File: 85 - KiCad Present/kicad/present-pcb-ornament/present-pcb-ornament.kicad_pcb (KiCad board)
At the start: 2 copper layers, 91.4 x 96.4 mm, 2 parts

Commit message: post stream
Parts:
- removed G*** (x2): LOGO, vector-files:inside zones
- added Ref**: Val**, svg2shen export:inky escaped, F.Cu at (157.7, 100.6)
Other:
- board size 91.4 x 96.4 mm -> 62.8 x 74.6 mm

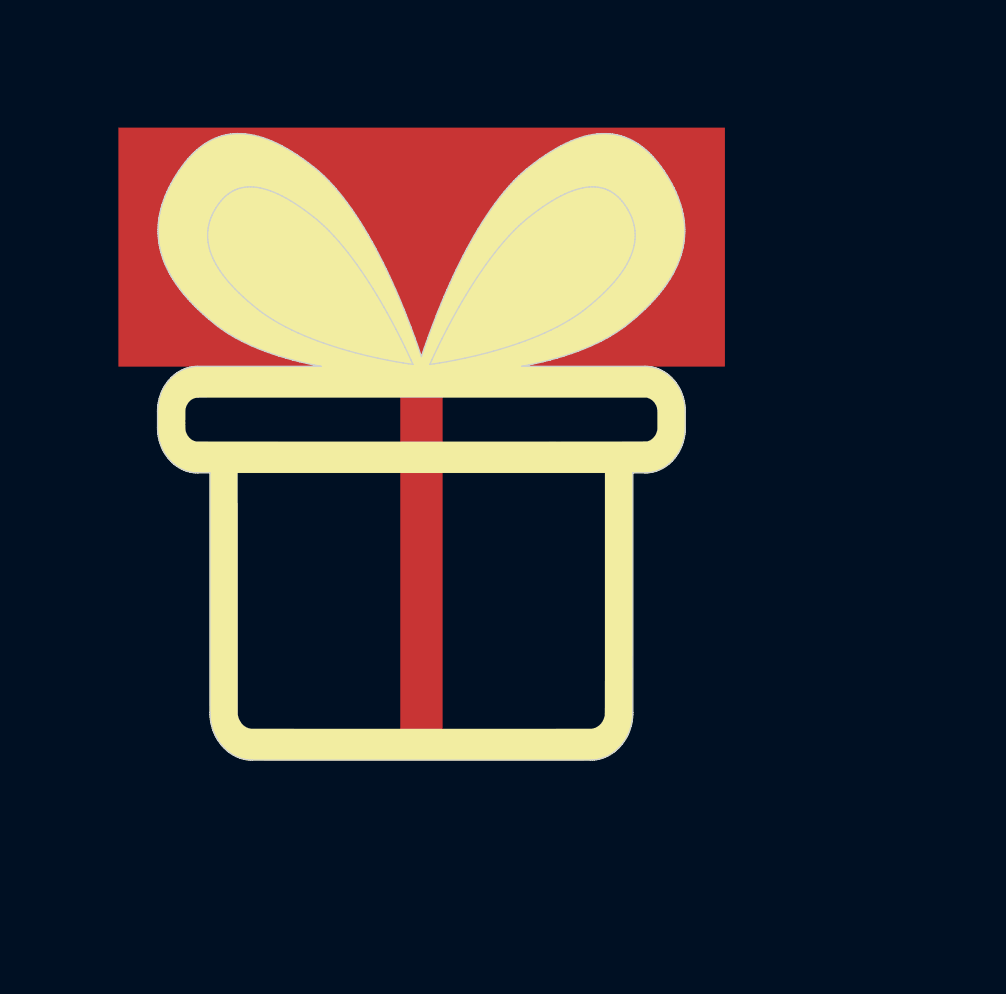
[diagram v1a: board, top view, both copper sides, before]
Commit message: new approach: atmega8 design
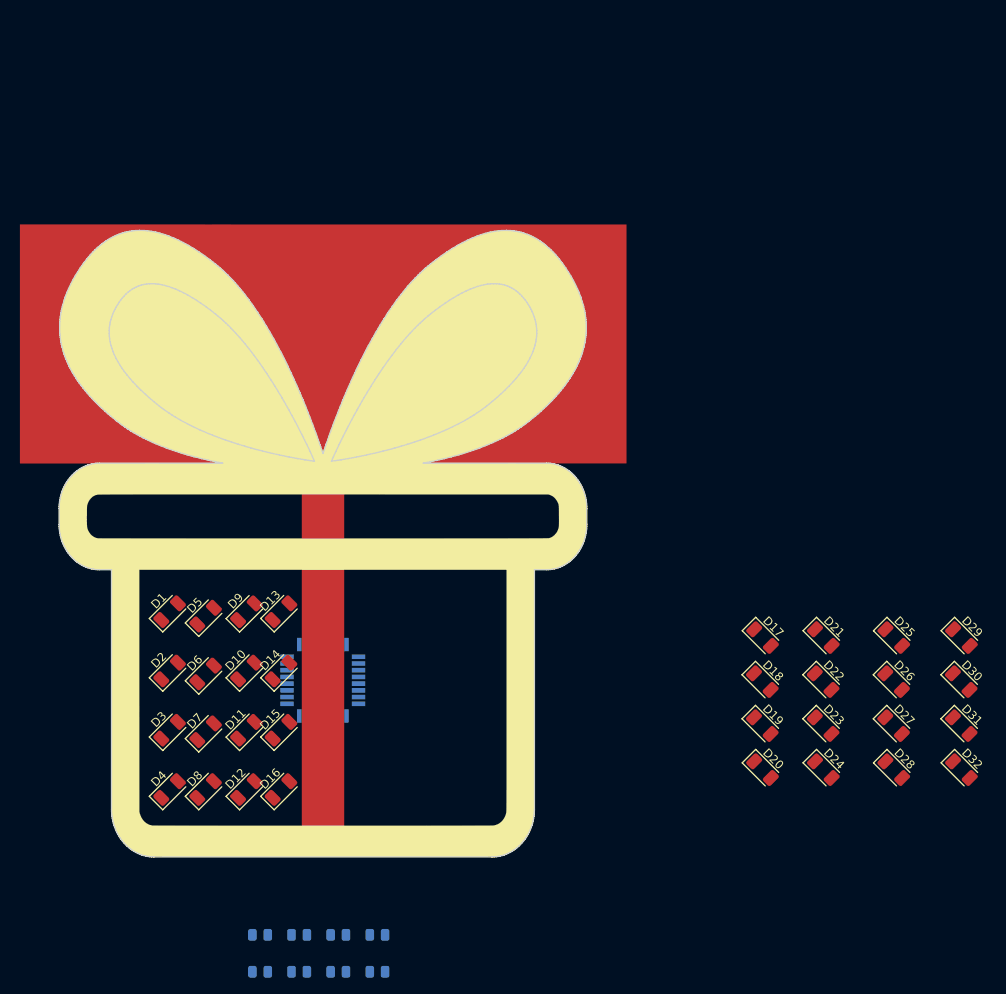
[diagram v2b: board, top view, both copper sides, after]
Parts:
- removed Ref**: Val**, svg2shen export:inky escaped
- added D1: GRN, LED_SMD:LED_1206_3216Metric, F.Cu at (129.1, 122.6)
- added D10: GRN, LED_SMD:LED_1206_3216Metric, F.Cu at (138.3, 129.7)
- added D11: GRN, LED_SMD:LED_1206_3216Metric, F.Cu at (138.3, 136.7)
- added D12: GRN, LED_SMD:LED_1206_3216Metric, F.Cu at (138.3, 143.8)
- added D13: GRN, LED_SMD:LED_1206_3216Metric, F.Cu at (142.4, 122.6)
- added D14: GRN, LED_SMD:LED_1206_3216Metric, F.Cu at (142.4, 129.7)
- added D15: GRN, LED_SMD:LED_1206_3216Metric, F.Cu at (142.4, 136.7)
- added D16: GRN, LED_SMD:LED_1206_3216Metric, F.Cu at (142.4, 143.8)
- added D17: GRN, LED_SMD:LED_1206_3216Metric, F.Cu at (199.7, 125.7)
- added D18: GRN, LED_SMD:LED_1206_3216Metric, F.Cu at (199.7, 130.9)
- added D19: GRN, LED_SMD:LED_1206_3216Metric, F.Cu at (199.7, 136.2)
- added D2: GRN, LED_SMD:LED_1206_3216Metric, F.Cu at (129.1, 129.7)
- added D20: GRN, LED_SMD:LED_1206_3216Metric, F.Cu at (199.7, 141.4)
- added D21: GRN, LED_SMD:LED_1206_3216Metric, F.Cu at (206.9, 125.7)
- added D22: GRN, LED_SMD:LED_1206_3216Metric, F.Cu at (206.9, 130.9)
- added D23: GRN, LED_SMD:LED_1206_3216Metric, F.Cu at (206.9, 136.2)
- added D24: GRN, LED_SMD:LED_1206_3216Metric, F.Cu at (206.9, 141.4)
- added D25: GRN, LED_SMD:LED_1206_3216Metric, F.Cu at (215.3, 125.7)
- added D26: GRN, LED_SMD:LED_1206_3216Metric, F.Cu at (215.3, 130.9)
- added D27: GRN, LED_SMD:LED_1206_3216Metric, F.Cu at (215.3, 136.2)
- added D28: GRN, LED_SMD:LED_1206_3216Metric, F.Cu at (215.3, 141.4)
- added D29: GRN, LED_SMD:LED_1206_3216Metric, F.Cu at (223.4, 125.7)
- added D3: GRN, LED_SMD:LED_1206_3216Metric, F.Cu at (129.1, 136.7)
- added D30: GRN, LED_SMD:LED_1206_3216Metric, F.Cu at (223.4, 130.9)
- added D31: GRN, LED_SMD:LED_1206_3216Metric, F.Cu at (223.4, 136.2)
- added D32: GRN, LED_SMD:LED_1206_3216Metric, F.Cu at (223.4, 141.4)
- added D4: GRN, LED_SMD:LED_1206_3216Metric, F.Cu at (129.1, 143.8)
- added D5: GRN, LED_SMD:LED_1206_3216Metric, F.Cu at (133.4, 123.1)
- added D6: GRN, LED_SMD:LED_1206_3216Metric, F.Cu at (133.4, 130.0)
- added D7: GRN, LED_SMD:LED_1206_3216Metric, F.Cu at (133.4, 136.9)
- added D8: GRN, LED_SMD:LED_1206_3216Metric, F.Cu at (133.4, 143.8)
- added D9: GRN, LED_SMD:LED_1206_3216Metric, F.Cu at (138.3, 122.6)
- added H1: PCB, svg2shen export:inky escaped, F.Cu at (146.0, 112.1)
- added R1: R_0805, Resistor_SMD:R_0805_2012Metric, B.Cu at (153.9, 161.1)
- added R2: R_0805, Resistor_SMD:R_0805_2012Metric, B.Cu at (149.2, 161.1)
- added R3: R_0805, Resistor_SMD:R_0805_2012Metric, B.Cu at (144.6, 161.1)
- added R4: R_0805, Resistor_SMD:R_0805_2012Metric, B.Cu at (139.9, 161.1)
- added R5: R_0805, Resistor_SMD:R_0805_2012Metric, B.Cu at (153.9, 165.5)
- added R6: R_0805, Resistor_SMD:R_0805_2012Metric, B.Cu at (149.2, 165.5)
- added R7: R_0805, Resistor_SMD:R_0805_2012Metric, B.Cu at (144.6, 165.5)
- added R8: R_0805, Resistor_SMD:R_0805_2012Metric, B.Cu at (139.9, 165.5)
- added U1: ATmega8A-AU, Package_QFP:TQFP-32_7x7mm_P0.8mm, B.Cu at (147.4, 130.8)
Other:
- outline, holes or cut-outs redrawn

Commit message: Stupid GND is Stupid
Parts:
- added C1: 10u, Capacitor_SMD:C_0805_2012Metric, B.Cu at (145.8, 126.0)
- added C2: 10u, Capacitor_SMD:C_0805_2012Metric, B.Cu at (138.0, 108.1)
- added D33: Batt, My Libraries:LED_1206_3216Metric-NoSilk, B.Cu at (139.4, 126.2)
- added D34: RED, My Libraries:LED_1206_3216Metric-NoSilk, F.Cu at (122.9, 111.3)
- added D35: RED, My Libraries:LED_1206_3216Metric-NoSilk, F.Cu at (129.1, 111.3)
- added D36: RED, My Libraries:LED_1206_3216Metric-NoSilk, F.Cu at (135.3, 111.3)
- added D37: RED, My Libraries:LED_1206_3216Metric-NoSilk, F.Cu at (141.5, 111.3)
- added D38: RED, My Libraries:LED_1206_3216Metric-NoSilk, F.Cu at (153.2, 111.3)
- added D39: RED, My Libraries:LED_1206_3216Metric-NoSilk, F.Cu at (159.3, 111.3)
- added D40: RED, My Libraries:LED_1206_3216Metric-NoSilk, F.Cu at (165.5, 111.3)
- added D41: RED, My Libraries:LED_1206_3216Metric-NoSilk, F.Cu at (171.7, 111.3)
- added J1: Batt, Connector_JST:JST_PH_S2B-PH-SM4-TB_1x02-1MP_P2.00mm_Horizontal, B.Cu at (146.2, 109.5)
- added J2: ISP, My Libraries:PinHeader_1x06_P2.54mm_SMD_Field, B.Cu at (124.5, 132.6)
- added R10: 0, Resistor_SMD:R_1206_3216Metric, B.Cu at (131.1, 116.3)
- added R11: 0, Resistor_SMD:R_1206_3216Metric, B.Cu at (135.8, 116.2)
- added R12: 0, Resistor_SMD:R_1206_3216Metric, B.Cu at (128.4, 116.2)
- added R13: 0, Resistor_SMD:R_1206_3216Metric, B.Cu at (173.6, 113.0)
- added R14: 0, Resistor_SMD:R_1206_3216Metric, B.Cu at (129.0, 107.2)
- added R15: 0, Resistor_SMD:R_1206_3216Metric, B.Cu at (118.5, 126.6)
- added R16: 0, Resistor_SMD:R_0805_2012Metric, B.Cu at (141.4, 128.7)
- added R17: 0, Resistor_SMD:R_0805_2012Metric, B.Cu at (148.7, 129.3)
- added R18: 0, Resistor_SMD:R_0805_2012Metric, B.Cu at (148.7, 135.8)
- added R19: 0, Resistor_SMD:R_1206_3216Metric, B.Cu at (140.2, 108.1)
- added R9: 1K, Resistor_SMD:R_0805_2012Metric, B.Cu at (135.0, 126.4)
- added SW1: PWR, My Libraries:SW_SPDT_PCM12-no-mounts, B.Cu at (156.7, 107.2)
- added SW2: RESET, My Libraries:SW_Push_CK_PTS525_SM15, B.Cu at (120.8, 111.1)
- D1: value GRN -> RED; footprint LED_SMD:LED_1206_3216Metric -> My Libraries:LED_1206_3216Metric-NoSilk
- D10, D11, D12, D13, D14, D15, D16, D17, D18, D19, D2, D20, D21, D22, D23, D24, D25, D26, D27, D28, D29, D3, D30, D31, D32, D4, D5, D6, D7, D8, D9: footprint LED_SMD:LED_1206_3216Metric -> My Libraries:LED_1206_3216Metric-NoSilk
- moved D29 57.4 mm to (166.0, 122.6)
- moved D32 57.4 mm to (166.0, 143.8)
- moved D30 57.4 mm to (166.0, 129.7)
- moved D31 57.3 mm to (166.0, 136.8)
- moved R8 54.6 mm to (166.1, 117.6)
- moved D25 53.8 mm to (161.6, 122.6)
- moved D28 53.8 mm to (161.6, 143.8)
- moved D26 53.7 mm to (161.6, 129.7)
- moved D27 53.7 mm to (161.6, 136.8)
- moved R7 50.8 mm to (161.5, 117.6)
- moved D21 49.9 mm to (157.2, 122.6)
- moved D24 49.8 mm to (157.2, 143.8)
- moved D22 49.8 mm to (157.2, 129.7)
- moved D23 49.7 mm to (157.2, 136.8)
- moved R5 48.9 mm to (153.4, 116.6), turned to 270 degrees
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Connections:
- net /Pin14 renamed Net-(U1-Pad2)
- net Net-(D1-Pad2) renamed /nR1
- net Net-(D10-Pad2) renamed /nR3
- net Net-(D13-Pad2) renamed /nR4
- net Net-(D17-Pad2) renamed /nR5
- net Net-(D21-Pad2) renamed /nR6
- net Net-(D25-Pad2) renamed /nR7
- net Net-(D29-Pad2) renamed /nR8
- net Net-(D5-Pad2) renamed /nR2
- D1 pad 1: /Pin9 -> /Pin10
- D10 pad 1: /Pin10 -> /Pin11
- D11 pad 1: /Pin11 -> /Pin12
- D12 pad 1: /Pin12 -> /Pin13
- D13 pad 1: /Pin9 -> /Pin10
- D14 pad 1: /Pin10 -> /Pin11
- D15 pad 1: /Pin11 -> /Pin12
- D16 pad 1: /Pin12 -> /Pin13
- D17 pad 1: /Pin9 -> /Pin10
- D18 pad 1: /Pin10 -> /Pin11
- D19 pad 1: /Pin11 -> /Pin12
- D2 pad 1: /Pin10 -> /Pin11
- D20 pad 1: /Pin12 -> /Pin13
- D21 pad 1: /Pin9 -> /Pin10
- D22 pad 1: /Pin10 -> /Pin11
- D23 pad 1: /Pin11 -> /Pin12
- D24 pad 1: /Pin12 -> /Pin13
- D25 pad 1: /Pin9 -> /Pin10
- D26 pad 1: /Pin10 -> /Pin11
- D27 pad 1: /Pin11 -> /Pin12
- D28 pad 1: /Pin12 -> /Pin13
- D29 pad 1: /Pin9 -> /Pin10
- D3 pad 1: /Pin11 -> /Pin12
- D30 pad 1: /Pin10 -> /Pin11
- D31 pad 1: /Pin11 -> /Pin12
- D32 pad 1: /Pin12 -> /Pin13
- D4 pad 1: /Pin12 -> /Pin13
- D5 pad 1: /Pin9 -> /Pin10
- D6 pad 1: /Pin10 -> /Pin11
- D7 pad 1: /Pin11 -> /Pin12
- D8 pad 1: /Pin12 -> /Pin13
- D9 pad 1: /Pin9 -> /Pin10
- U1 pad 10: /Pin16 -> /Pin3
- U1 pad 11: /Pin17 -> /Pin2
- U1 pad 13: /Pin2 -> Net-(U1-Pad13)
- U1 pad 14: /Pin3 -> Net-(U1-Pad14)
- U1 pad 18: Net-(U1-Pad18) -> VDD
- U1 pad 19: Net-(U1-Pad19) -> VDD
- U1 pad 20: Net-(U1-Pad20) -> VDD
- U1 pad 21: Net-(U1-Pad21) -> GND
- U1 pad 24: /Pin5 -> /Pin9
- U1 pad 25: /Pin6 -> /Pin8
- U1 pad 27: /Pin8 -> /Pin6
- U1 pad 28: /Pin9 -> /Pin5
- U1 pad 29: Net-(U1-Pad29) -> /RESET
- U1 pad 3: Net-(U1-Pad3) -> GND
- U1 pad 4: Net-(U1-Pad4) -> VDD
- U1 pad 5: Net-(U1-Pad3) -> GND
- U1 pad 6: Net-(U1-Pad4) -> VDD
- U1 pad 9: /Pin15 -> /Pin17
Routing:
- net /nR5: track 0.00 -> 191.2 mm, vias 0 -> 5
- net /nR6: track 0.00 -> 147.5 mm, vias 0 -> 5
- net /RESET: track 0.00 -> 112.5 mm
- net /Pin9: track 0.00 -> 108.2 mm, vias 0 -> 8
- net /nR7: track 0.00 -> 106.4 mm, vias 0 -> 5
- net /nR4: track 0.00 -> 101.4 mm, vias 0 -> 5
- net /nR3: track 0.00 -> 92.7 mm, vias 0 -> 5
- net VDD: track 0.00 -> 83.4 mm
- net /Pin4: track 0.00 -> 68.9 mm
- net /nR2: track 0.00 -> 68.3 mm, vias 0 -> 5
- net /Pin13: track 0.00 -> 58.1 mm, vias 0 -> 8
- net /Pin10: track 0.00 -> 55.2 mm, vias 0 -> 8
- net GND: track 0.00 -> 52.7 mm
- net /Pin12: track 0.00 -> 51.8 mm, vias 0 -> 8
- net /nR1: track 0.00 -> 50.7 mm, vias 0 -> 5
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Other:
- net class Default: clearance 0.2 -> 0.1524; trace_width 0.25 -> 0.1524
- rule trace_clearance: 0.2 -> 0.1524
- rule trace_min: 0.2 -> 0.127

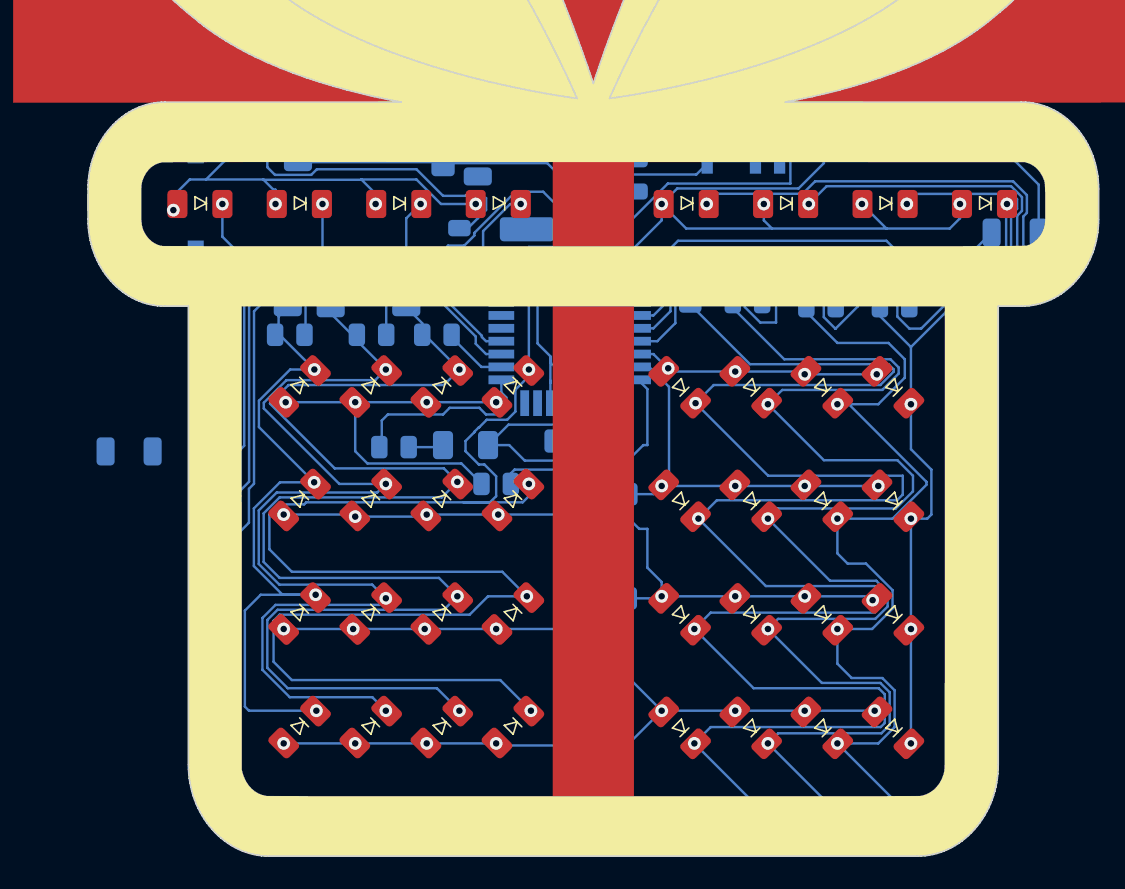
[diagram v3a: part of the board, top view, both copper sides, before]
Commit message: Got GND. 9 remaining routes are the 0 ohm shorts.
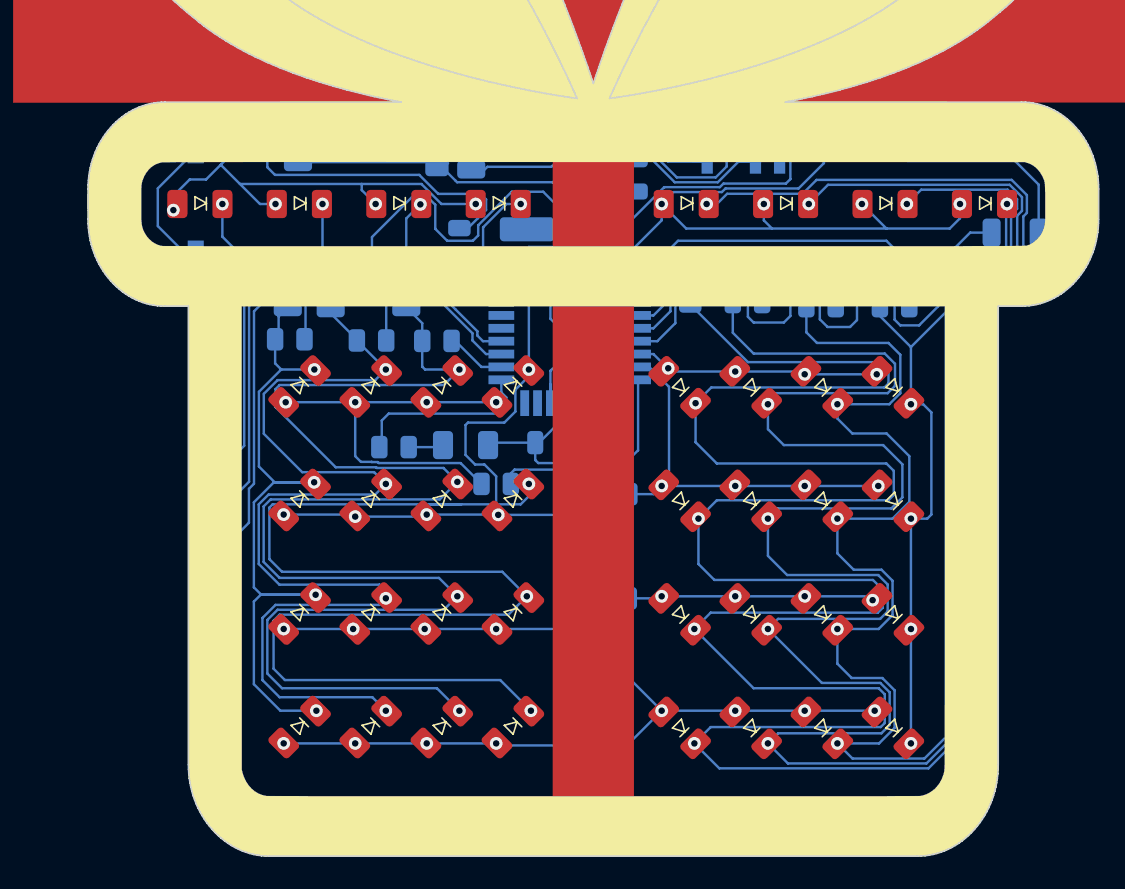
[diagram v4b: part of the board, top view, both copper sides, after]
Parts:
- removed R15: 0, Resistor_SMD:R_1206_3216Metric
- moved C1 1.07 mm to (144.7, 126.1), turned to 180 degrees
- moved R19 0.59 mm to (139.8, 107.6)
- moved C2 0.38 mm to (137.7, 108.1)
- moved R3 0.38 mm to (137.7, 119.8)
- moved R2 0.36 mm to (133.6, 119.7)
- moved R1 0.28 mm to (128.5, 119.7)
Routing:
- net GND: track 52.7 -> 94.2 mm
- net /RESET: track 112.5 -> 120.0 mm
- net /SCK: track 39.4 -> 44.2 mm
- net VDD: track 83.4 -> 87.5 mm
- net /nR5: track 191.2 -> 187.4 mm
- net /nR7: track 106.4 -> 104.0 mm
- net /nR2: track 68.3 -> 70.4 mm
- net /nR4: track 101.4 -> 103.4 mm
- net /Pin12: track 51.8 -> 50.2 mm
- net /nR6: track 147.5 -> 146.0 mm
- net /nR3: track 92.7 -> 94.1 mm
- net /Pin9: track 108.2 -> 106.9 mm
